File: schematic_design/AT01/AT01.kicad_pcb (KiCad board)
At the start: 2 copper layers, 85 x 56 mm, 57 parts, among them J1 JST Connector, J2 Conn_01x08, J3 USB_C_Receptacle_USB2.0, J4 DC Pump Connector, J5 Solenoid Valve Connector, Q1 DMG2301L, Q2 2N7002, Q3 2N7002, SW1 SW_Push, SW2 SW_Push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

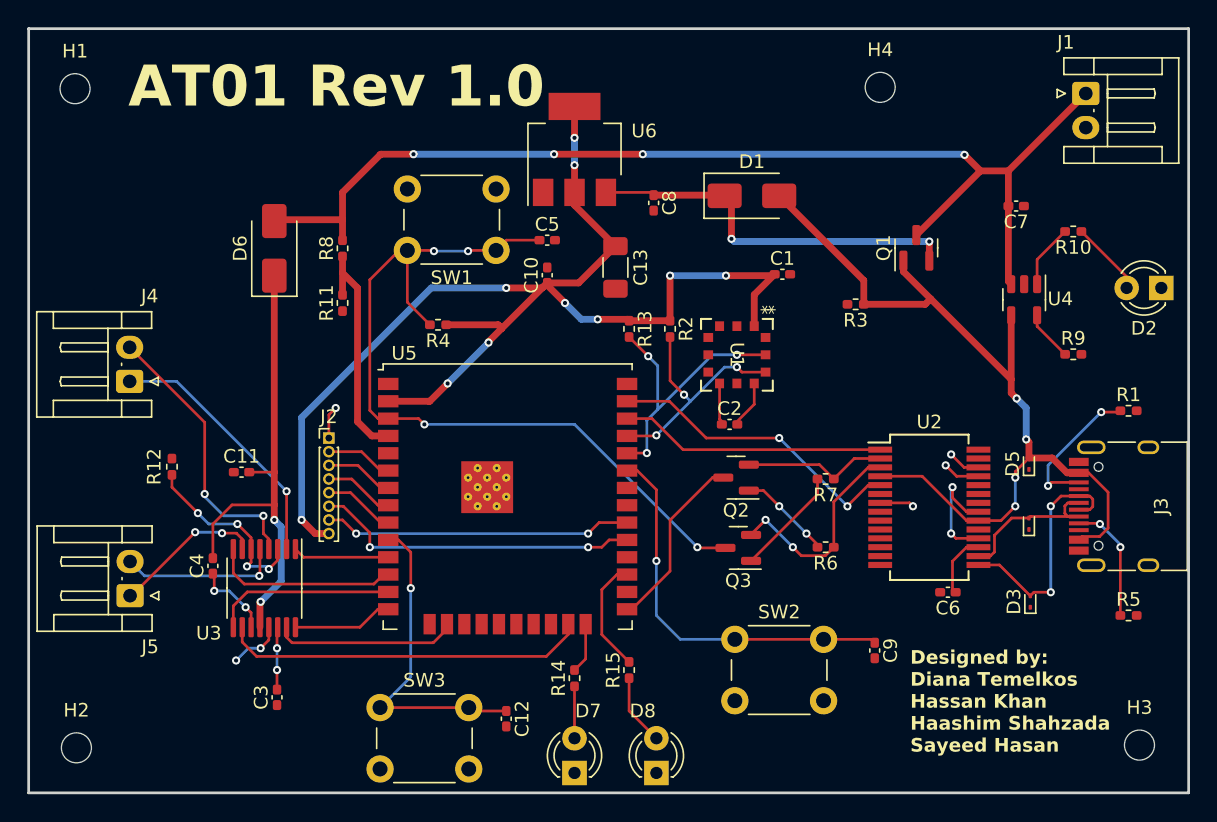
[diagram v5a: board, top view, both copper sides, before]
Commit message: moving gnd panel to back copper, button modifications
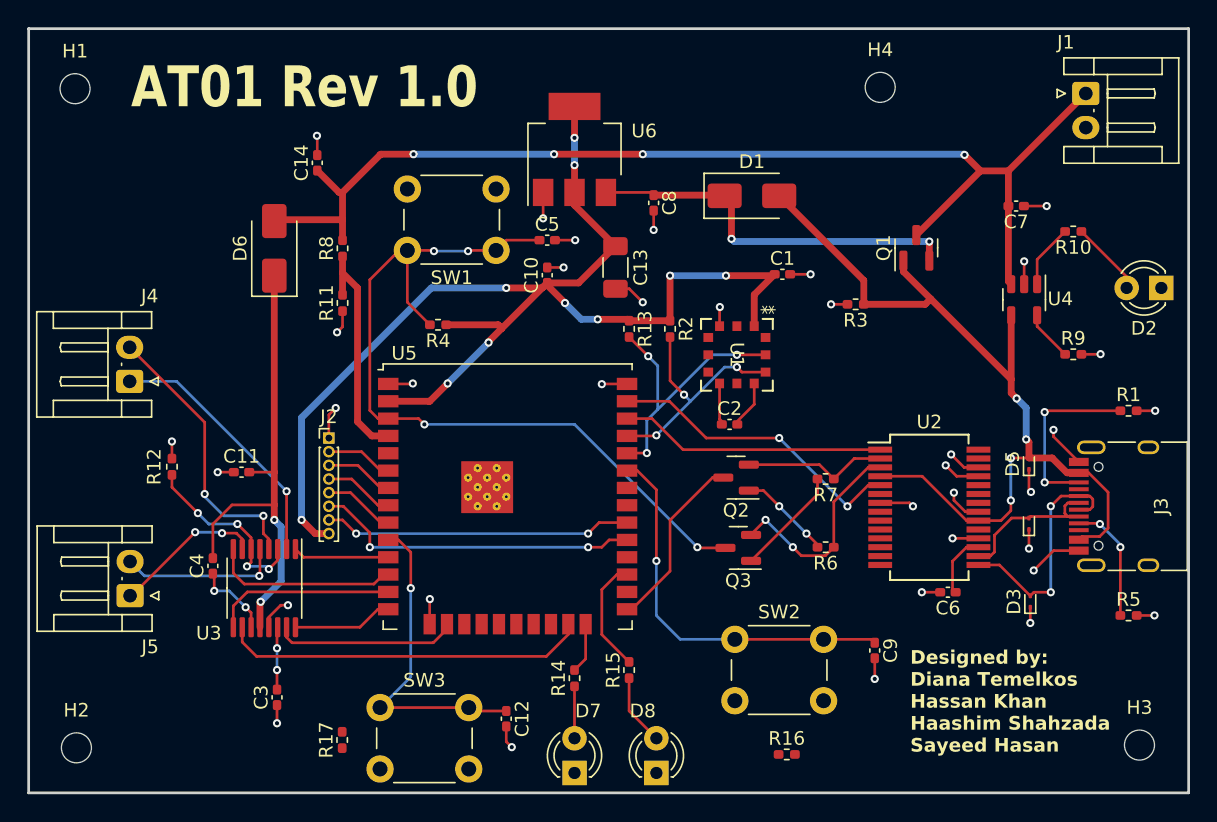
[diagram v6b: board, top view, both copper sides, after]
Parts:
- added C14: 100uF, Capacitor_SMD:C_0402_1005Metric_Pad0.74x0.62mm_HandSolder, F.Cu at (126.2, 81.8)
- added R16: 10K, Resistor_SMD:R_0402_1005Metric_Pad0.72x0.64mm_HandSolder, F.Cu at (160.6, 125.2)
- added R17: 10K, Resistor_SMD:R_0402_1005Metric_Pad0.72x0.64mm_HandSolder, F.Cu at (128.0, 124.1)
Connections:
- C12 pad 2: GND -> Net-(C12-Pad2)
- C9 pad 2: GND -> Net-(C9-Pad2)
- SW2 pad 2: GND -> Net-(C9-Pad2)
- SW3 pad 2: GND -> Net-(C12-Pad2)
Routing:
- net GND: track 22.7 -> 62.1 mm, vias 8 -> 34
- net Net-(J3-CC2): track 10.8 -> 13.4 mm
- net VBAT: track 81.7 -> 84.2 mm
- net Net-(C12-Pad2): track 0.00 -> 1.68 mm, vias 0 -> 1
- net Net-(C9-Pad2): track 0.00 -> 1.52 mm, vias 0 -> 1
- net VBUS: track 66.2 -> 66.9 mm
- added copper zone on B.Cu, net GND
- removed copper zone on F.Cu, net GND

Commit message: adding board with direct USB-C connection, esp32-s3 based
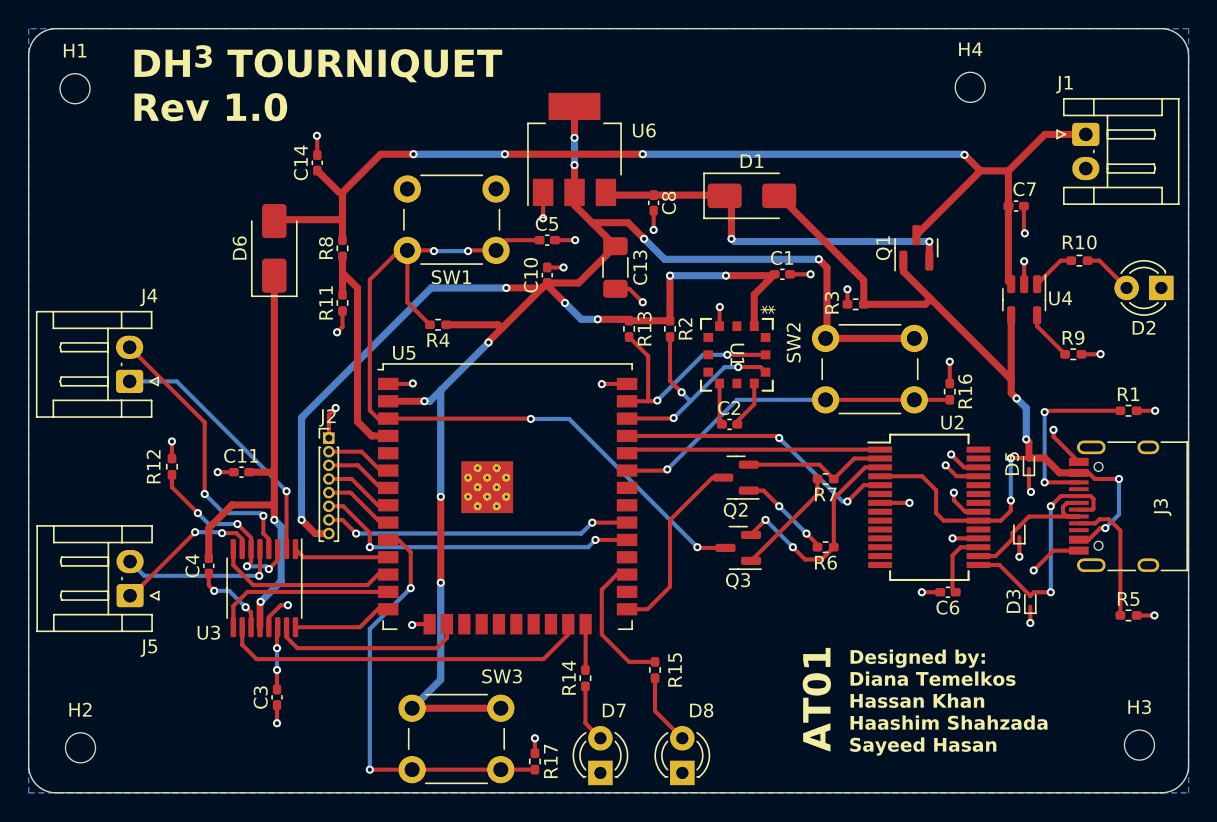
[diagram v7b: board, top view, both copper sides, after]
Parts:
- removed C12, C9: 1uF, Capacitor_SMD:C_0402_1005Metric_Pad0.74x0.62mm_HandSolder
- moved R16 29.1 mm to (172.5, 98.6), turned to -90 degrees
- moved SW2 23.0 mm to (163.4, 94.7)
- moved R17 14.2 mm to (142.1, 125.7), turned to -90 degrees
- moved H4 6.60 mm to (174.0, 76.3)
- moved J1 3.00 mm to (182.5, 79.8)
- moved SW3 2.35 mm to (133.1, 121.8)
- moved R10 2.18 mm to (182.0, 89.0)
- moved D7 1.90 mm to (146.9, 126.5)
- moved D8 1.90 mm to (152.9, 126.5)
- moved R15 1.90 mm to (150.9, 119.0)
- moved D4 0.92 mm to (177.6, 108.9)
- moved R14 0.80 mm to (145.8, 119.6)
- moved C4 0.30 mm to (118.2, 111.4)
- moved H2 0.30 mm to (108.8, 124.7)
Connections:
- R16 pad 1: unconnected-(R16-Pad1) -> GND
- R16 pad 2: Net-(C9-Pad2) -> Net-(U5-IO21)
- R17 pad 2: Net-(C12-Pad2) -> Net-(U5-IO25)
- SW2 pad 1: Net-(U5-IO21) -> 3V3
- SW2 pad 2: Net-(C9-Pad2) -> Net-(U5-IO21)
- SW3 pad 1: Net-(U5-IO25) -> 3V3
- SW3 pad 2: Net-(C12-Pad2) -> Net-(U5-IO25)
- U5 pad 34: SDA -> RXD0
- U5 pad 35: SCL -> TXD0
- U5 pad 36: RXD0 -> SCL
- U5 pad 37: TXD0 -> SDA
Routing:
- net 3V3: track 94.7 -> 155.7 mm, vias 10 -> 14
- net Net-(U5-IO25): track 23.7 -> 31.3 mm, vias 1 -> 2
- net SDA: track 20.9 -> 16.9 mm, vias 3 -> 2
- net Net-(U5-IO21): track 28.8 -> 25.8 mm
- net VBUS: track 66.9 -> 69.5 mm, vias 4 -> 6
- net GND: track 62.1 -> 64.2 mm, vias 34 -> 36
- net Net-(U5-IO16): track 8.43 -> 10.3 mm
- net Net-(D2-A): track 5.51 -> 3.69 mm
- net Net-(C12-Pad2): track 1.68 -> 0.00 mm, vias 1 -> 0
- net Net-(C9-Pad2): track 1.52 -> 0.00 mm, vias 1 -> 0
- net Net-(U4-STAT): track 4.71 -> 3.22 mm
- net TXD0: track 22.4 -> 21.0 mm
- net VBAT: track 84.2 -> 83.0 mm
- net Net-(J3-CC1): track 8.89 -> 9.73 mm, vias 2 -> 0
- net RXD0: track 19.5 -> 18.7 mm
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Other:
- outline, holes or cut-outs redrawn
- board text added: "AT01"
- board text added: "DH^{3} TOURNIQUET Rev 1.0"
- board text removed: "AT01 Rev 1.0"

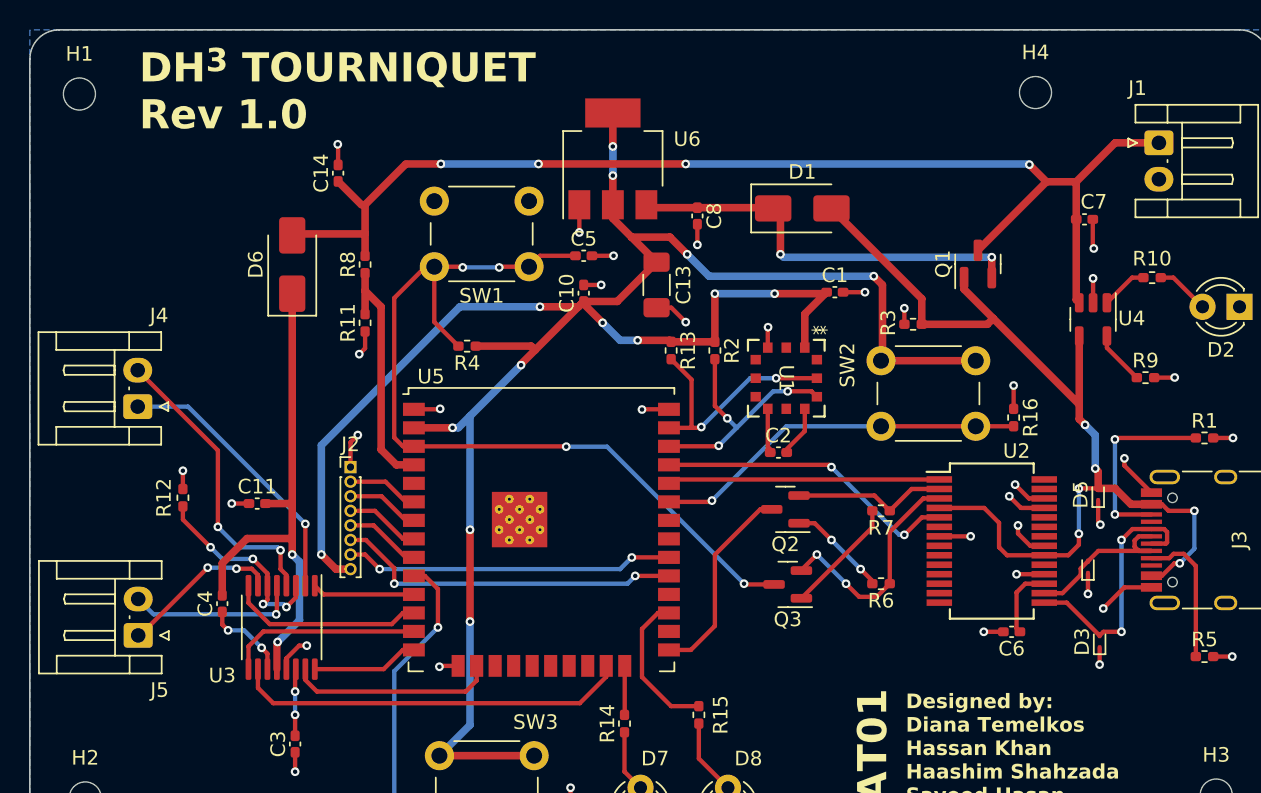
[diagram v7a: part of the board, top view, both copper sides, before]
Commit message: added redesigned charging circuit
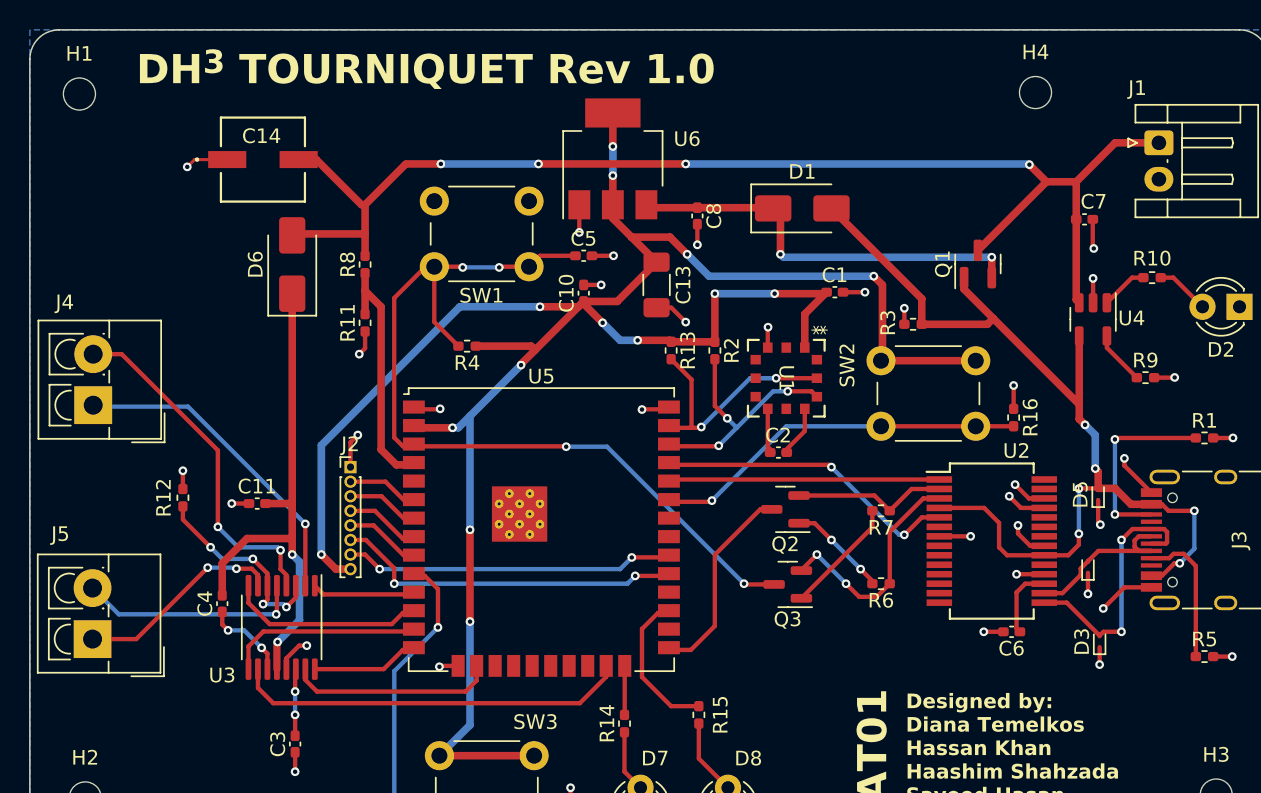
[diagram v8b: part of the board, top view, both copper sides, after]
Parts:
- C14: footprint Capacitor_SMD:C_0402_1005Metric_Pad0.74x0.62mm_HandSolder -> Library:CAP_FN_C_PAN
- J4, J5: footprint Connector_JST:JST_EH_S2B-EH_1x02_P2.50mm_Horizontal -> TerminalBlock_4Ucon:TerminalBlock_4Ucon_1x02_P3.50mm_Vertical
- U5: footprint RF_Module:ESP32-WROOM-32U -> RF_Module:ESP32-WROOM-32UE
- moved C14 5.24 mm to (121.0, 80.9), turned to 0 degrees
- moved J5 3.14 mm to (109.3, 113.8)
- moved J4 3.06 mm to (109.3, 97.8)
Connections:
- C14 pad 1: VBAT -> GND
- C14 pad 2: GND -> VBAT
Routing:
- net Net-(J4-Pin_2): track 20.6 -> 24.1 mm
- net Net-(J5-Pin_2): track 11.9 -> 15.3 mm
- net VBAT: track 83.0 -> 86.3 mm
- net Net-(J5-Pin_1): track 11.1 -> 14.3 mm
- net Net-(J4-Pin_1): track 19.1 -> 22.2 mm
- net GND: track 64.2 -> 65.7 mm
